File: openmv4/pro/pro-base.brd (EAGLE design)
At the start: 35.6 x 44.5 mm, 180 parts, among them J2 SAMTEC_FTSH-105-01-F-DVSAMTEC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, J6 RSP-122811-01, M1 9774030243R, M2 9774030243R, Q1 BSS138, Q2 AO3401, U1 W25Q256JVEIQ_TR, U10 STM32H743IIK6, U11 TEXAS_INSTRUMENTS_BQ24072TRGT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, U12 MICROCHIP_ATECC608A-SSHDA-BMI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, U14 IS42S32800, U2 EMIF06-MSD02N16, U3 ME6211C18M5G, U4 PAM2305AABADJ, U5 LSM6DS3TR-C, U6 MICROCHIP_USB3320C-EZK-TRMICR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, U7 LBEE5KL1DX-TEMP, U9 VL53L5CX, X2 USD-1040310811, X3 DF12-36-DS, X4 S2B-PH-K-S(LF)(SN), Y0 SITIME_SIT1533AI-H4-DCC-32.76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, Y1 DSC1001BI1-024.0000

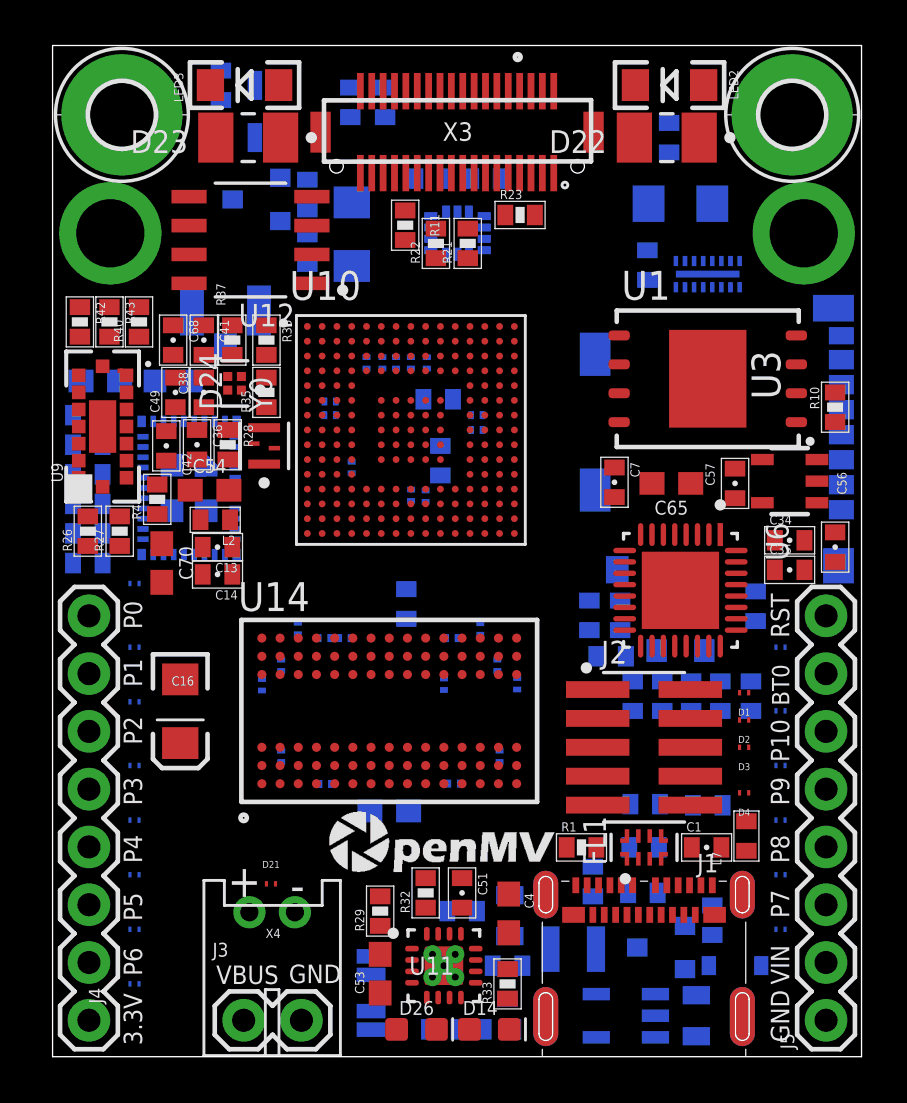
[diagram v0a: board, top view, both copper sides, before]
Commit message: Update jumpers to 0 ohm
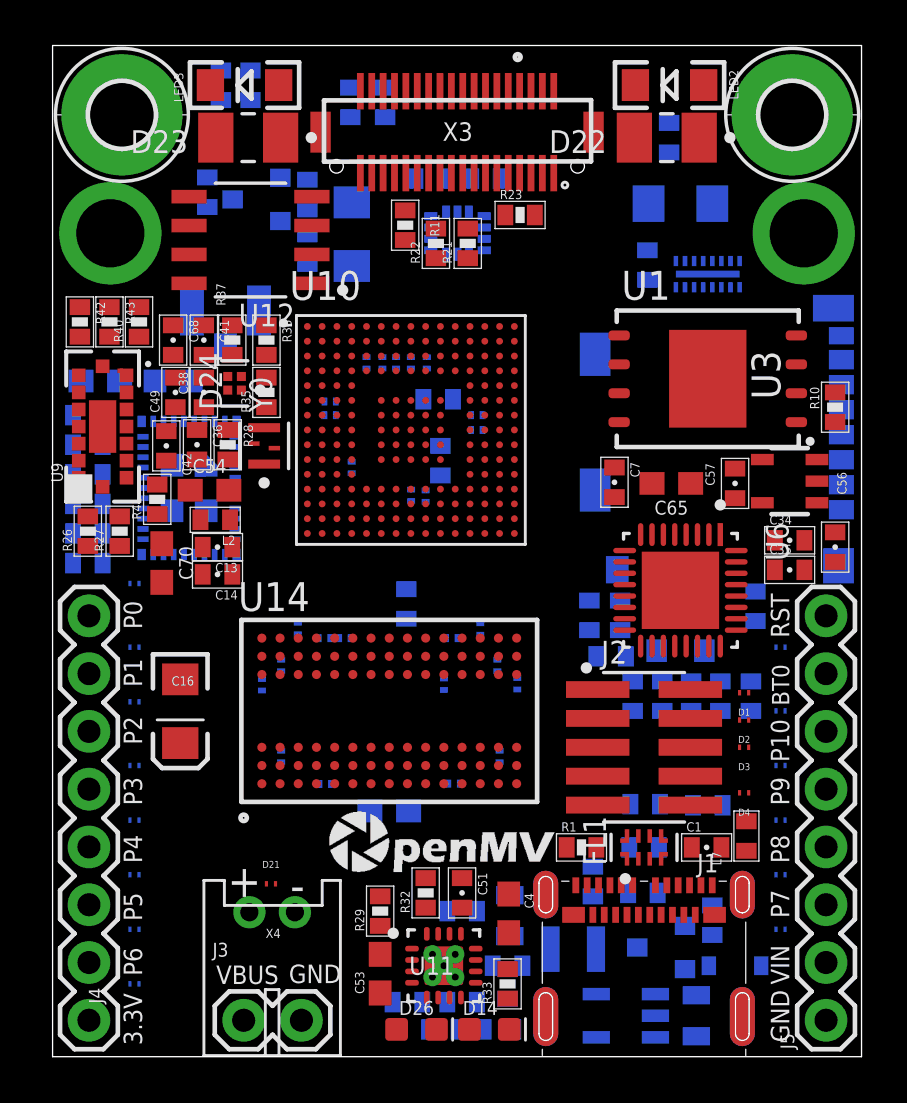
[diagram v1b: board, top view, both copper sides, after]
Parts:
- removed JP1, JP3, JP4: JUMPER-SMT_2_NC_PASTE_SILK, SparkFun-Jumpers:SMT-JUMPER_2_NC_PASTE_SILK
- removed JP2: JUMPER-SMT_2_NO_SILK, SparkFun-Jumpers:SMT-JUMPER_2_NO_SILK
- added R47, R49, R50: 0R, sfe:0402-RES
- added R48: 0R (DNP), sfe:0402-RES
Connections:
- removed net FLASH_!CS: R10.1, U1.1
- net FLASH_CS: now also R10.1, U1.1
- net LED_DRAIN: now also R48.1, R49.1; no longer JP1.1, JP2.1
- net LED_IR_DRIVE: now also R49.2; no longer JP1.2
- net LED_W_DRIVE: now also R48.2; no longer JP2.2
- net N$11: now also R47.1; no longer JP4.1
- net N$12: now also R50.1; no longer JP3.1
- net OUT: now also R47.2, R50.2; no longer JP3.2, JP4.2
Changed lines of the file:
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@@
 <attribute name="VALUE" x="6.257" y="39.3205" size="0.4064" layer="28" rot="MR90"/>
-</element>
-<element name="JP1" library="SparkFun-Jumpers" library_urn="urn:adsk.eagle:library:528" package="SMT-JUMPER_2_NC_PASTE_SILK" package3d_urn="urn:adsk.eagle:package:39282/1" value="JUMPER-SMT_2_NC_PASTE_SILK" x="9.3" y="42.7" smashed="yes" rot="MR0">
-<attribute name="NAME" x="9.3" y="43.843" size="0.6096" layer="26" font="vector" ratio="20" rot="MR0" align="bottom-center"/>
-<attribute name="VALUE" x="9.3" y="41.557" size="0.6096" layer="28" font="vector" ratio="20" rot="MR0" align="top-center"/>
-</element>
-<element name="JP2" library="SparkFun-Jumpers" library_urn="urn:adsk.eagle:library:528" package="SMT-JUMPER_2_NO_SILK" package3d_urn="urn:adsk.eagle:package:39279/1" value="JUMPER-SMT_2_NO_SILK" x="9.3" y="40.4" smashed="yes" rot="MR0">
-<attribute name="NAME" x="9.3" y="41.543" size="0.6096" layer="26" font="vector" ratio="20" rot="MR0" align="bottom-center"/>
-<attribute name="VALUE" x="9.3" y="39.257" size="0.6096" layer="28" font="vector" ratio="20" rot="MR0" align="top-center"/>
 </element>
 <element name="R35" library="sfe" package="0402-RES" value="220" x="9.4" y="29.2" smashed="yes" rot="R90">
@@
 <attribute name="VALUE" x="16" y="0.565" size="0.6096" layer="27" font="vector" ratio="20" align="top-center"/>
 </element>
-<element name="JP3" library="SparkFun-Jumpers" library_urn="urn:adsk.eagle:library:528" package="SMT-JUMPER_2_NC_PASTE_SILK" package3d_urn="urn:adsk.eagle:package:39282/1" value="JUMPER-SMT_2_NC_PASTE_SILK" x="14" y="1.6" smashed="yes" rot="MR90">
-<attribute name="NAME" x="15.143" y="1.6" size="0.6096" layer="26" font="vector" ratio="20" rot="MR90" align="bottom-center"/>
-<attribute name="VALUE" x="20" y="2.857" size="0.6096" layer="28" font="vector" ratio="20" rot="MR0" align="top-center"/>
-</element>
-<element name="JP4" library="SparkFun-Jumpers" library_urn="urn:adsk.eagle:library:528" package="SMT-JUMPER_2_NC_PASTE_SILK" package3d_urn="urn:adsk.eagle:package:39282/1" value="JUMPER-SMT_2_NC_PASTE_SILK" x="14" y="4" smashed="yes" rot="MR270">
-<attribute name="NAME" x="12.857" y="4" size="0.6096" layer="26" font="vector" ratio="20" rot="MR270" align="bottom-center"/>
-<attribute name="VALUE" x="20" y="5.143" size="0.6096" layer="28" font="vector" ratio="20" rot="MR180" align="top-center"/>
+<element name="R47" library="sfe" package="0402-RES" value="0R" x="18" y="2.4" smashed="yes" rot="MR0">
+<attribute name="NAME" x="18.889" y="3.0985" size="0.4064" layer="26" rot="MR0"/>
+<attribute name="VALUE" x="19.0795" y="1.257" size="0.4064" layer="28" rot="MR0"/>
+</element>
+<element name="R48" library="sfe" package="0402-RES" value="0R (DNP)" x="6.8" y="38" smashed="yes" rot="MR90">
+<attribute name="NAME" x="7.4985" y="37.111" size="0.4064" layer="26" rot="MR90"/>
+<attribute name="VALUE" x="5.657" y="36.9205" size="0.4064" layer="28" rot="MR90"/>
+</element>
+<element name="R49" library="sfe" package="0402-RES" value="0R" x="8.7" y="42.7" smashed="yes" rot="MR90">
+<attribute name="NAME" x="9.3985" y="41.811" size="0.4064" layer="26" rot="MR90"/>
+<attribute name="VALUE" x="7.557" y="41.6205" size="0.4064" layer="28" rot="MR90"/>
+</element>
+<element name="R50" library="sfe" package="0402-RES" value="0R" x="15.6" y="2.4" smashed="yes" rot="MR180">
+<attribute name="NAME" x="14.711" y="1.7015" size="0.4064" layer="26" rot="MR180"/>
+<attribute name="VALUE" x="14.5205" y="3.543" size="0.4064" layer="28" rot="MR180"/>
 </element>
 </elements>
@@
 <wire x1="24.905" y1="30.435" x2="11.2" y2="25.6" width="0" layer="19" extent="1-1"/>
 </signal>
-<signal name="FLASH_!CS">
-<contactref element="U1" pad="1"/>
-<contactref element="R10" pad="1"/>
-<wire x1="32.695" y1="27.895" x2="34.4" y2="27.9" width="0" layer="19" extent="1-1"/>
-</signal>
 <signal name="DAT0">
 <contactref element="X2" pad="P$7"/>
@@
 <signal name="FLASH_CS">
 <contactref element="U10" pad="J15"/>
+<contactref element="U1" pad="1"/>
+<contactref element="R10" pad="1"/>
+<wire x1="32.695" y1="27.895" x2="34.4" y2="27.9" width="0" layer="19" extent="1-1"/>
+<wire x1="20.3" y1="26.9" x2="32.695" y2="27.895" width="0" layer="19" extent="1-1"/>
 </signal>
 <signal name="SPI6_SSEL">
@@
 <contactref element="C4" pad="2"/>
 <contactref element="U11" pad="5"/>
-<contactref element="JP3" pad="2"/>
-<contactref element="JP4" pad="2"/>
+<contactref element="R47" pad="2"/>
+<contactref element="R50" pad="2"/>
 <wire x1="20.05" y1="5.45" x2="25.7" y2="4.8" width="0" layer="19" extent="1-16"/>
 <wire x1="18.6" y1="4.25" x2="20.05" y2="5.45" width="0" layer="19" extent="1-1"/>
 <wire x1="18.6" y1="3.75" x2="18.6" y2="4.25" width="0" layer="19" extent="1-1"/>
-<wire x1="16.45" y1="2.6" x2="18.6" y2="3.75" width="0" layer="19" extent="1-1"/>
-<wire x1="14" y1="2.0064" x2="16.45" y2="2.6" width="0" layer="19" extent="1-16"/>
-<wire x1="14" y1="3.5936" x2="14" y2="2.0064" width="0" layer="19" extent="16-16"/>
+<wire x1="17.35" y1="2.4" x2="18.6" y2="3.75" width="0" layer="19" extent="1-16"/>
+<wire x1="16.45" y1="2.6" x2="17.35" y2="2.4" width="0" layer="19" extent="1-16"/>
+<wire x1="16.25" y1="2.4" x2="16.45" y2="2.6" width="0" layer="19" extent="1-16"/>
 </signal>
 <signal name="LED_B_INT">
@@
 <contactref element="R2" pad="1"/>
 <contactref element="R31" pad="1"/>
-<contactref element="JP2" pad="2"/>
-<wire x1="8.8936" y1="40.4" x2="27.1" y2="41.05" width="0" layer="19" extent="16-16"/>
-<wire x1="7.4" y1="39.75" x2="8.8936" y2="40.4" width="0" layer="19" extent="16-16"/>
+<contactref element="R48" pad="2"/>
+<wire x1="7.4" y1="39.75" x2="27.1" y2="41.05" width="0" layer="19" extent="16-16"/>
+<wire x1="6.8" y1="38.65" x2="7.4" y2="39.75" width="0" layer="19" extent="16-16"/>
 </signal>
 <signal name="LED_DRAIN">
 <contactref element="Q1" pad="3"/>
-<contactref element="JP1" pad="1"/>
-<contactref element="JP2" pad="1"/>
-<wire x1="9.7064" y1="40.4" x2="9.7064" y2="42.7" width="0" layer="19" extent="16-16"/>
-<wire x1="7.912" y1="37.684" x2="9.7064" y2="40.4" width="0" layer="19" extent="16-16"/>
+<contactref element="R48" pad="1"/>
+<contactref element="R49" pad="1"/>
+<wire x1="7.912" y1="37.684" x2="8.7" y2="42.05" width="0" layer="19" extent="16-16"/>
+<wire x1="6.8" y1="37.35" x2="7.912" y2="37.684" width="0" layer="19" extent="16-16"/>
 </signal>
 <signal name="LED_IR_DRIVE">
-<contactref element="JP1" pad="2"/>
 <contactref element="R5" pad="1"/>
-<wire x1="8.8936" y1="42.7" x2="7.4" y2="43.35" width="0" layer="19" extent="1-16"/>
+<contactref element="R49" pad="2"/>
+<wire x1="7.4" y1="43.35" x2="8.7" y2="43.35" width="0" layer="19" extent="16-16"/>
 </signal>
 <signal name="LED_IR_INT">
@@
 <signal name="N$11">
 <contactref element="R33" pad="2"/>
-<contactref element="JP4" pad="1"/>
-<wire x1="14" y1="4.4064" x2="20" y2="3.85" width="0" layer="19" extent="1-16"/>
+<contactref element="R47" pad="1"/>
+<wire x1="18.65" y1="2.4" x2="20" y2="3.85" width="0" layer="19" extent="1-16"/>
 </signal>
 <signal name="N$12">
 <contactref element="R46" pad="2"/>
-<contactref element="JP3" pad="1"/>
-<wire x1="16.55" y1="1.2" x2="14" y2="1.1936" width="0" layer="19" extent="16-16"/>
+<contactref element="R50" pad="1"/>
+<wire x1="14.95" y1="2.4" x2="16.55" y2="1.2" width="0" layer="19" extent="16-16"/>
 </signal>
 </signals>
